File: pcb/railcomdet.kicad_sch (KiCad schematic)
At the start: 23 parts, among them J1 Screw_Terminal_01x04, J2 Screw_Terminal_01x02, J3 Screw_Terminal_01x08, U1 VO0631T, U15 VO0631T, U2 VO0631T

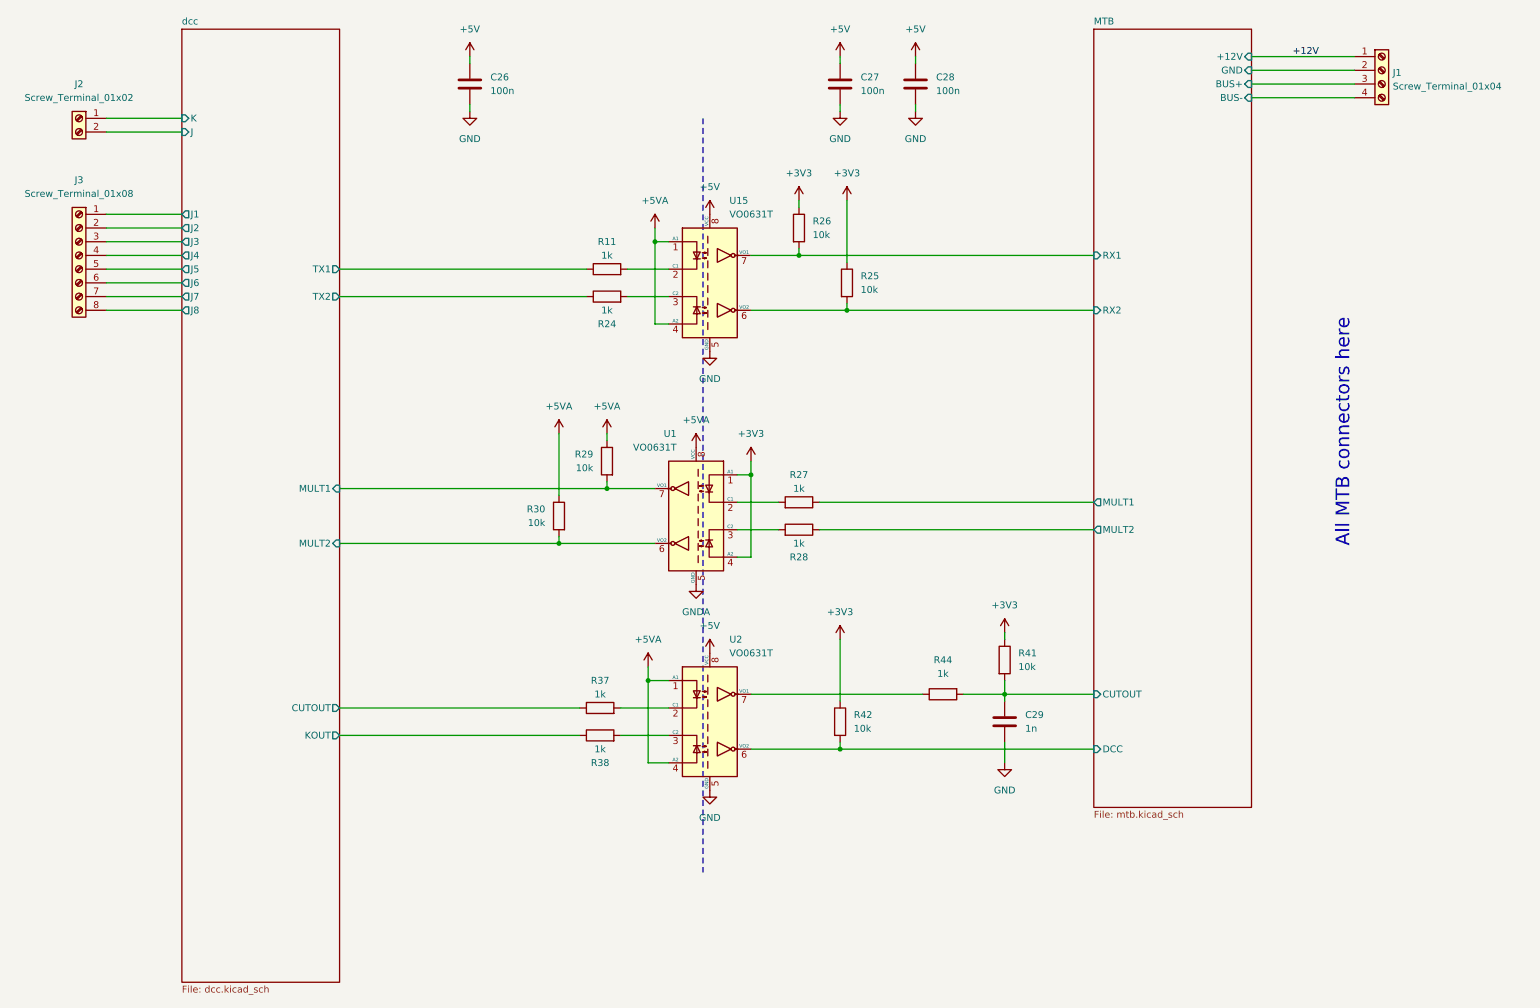
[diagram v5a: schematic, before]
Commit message: Added testpoints.
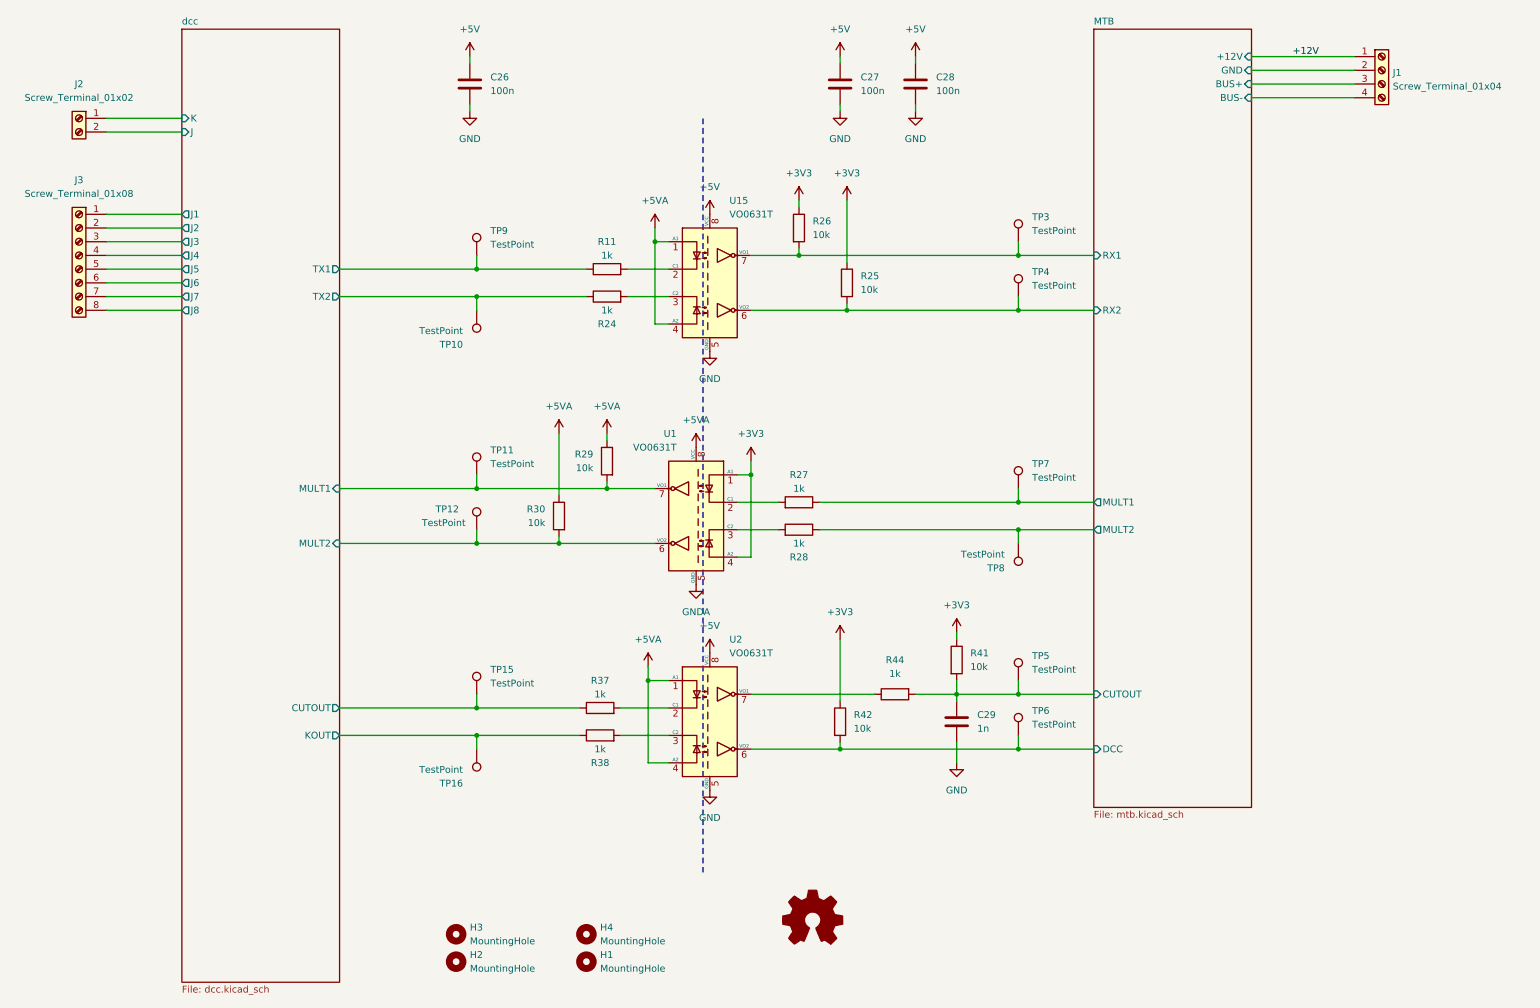
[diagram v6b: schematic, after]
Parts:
- added H1, H2, H3, H4: MountingHole, symbol Mechanical:MountingHole
- added TP10, TP11, TP12, TP15, TP16, TP3, TP4, TP5, TP6, TP7, TP8, TP9: TestPoint, symbol Connector:TestPoint
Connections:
- net MTB/CUTOUT: now also TP5.1
- net MTB/DCC: now also TP6.1
- net MTB/MULT1: now also TP7.1
- net MTB/MULT2: now also TP8.1
- net MTB/RX1: now also TP3.1
- net MTB/RX2: now also TP4.1
- net dcc/CUTOUT: now also TP15.1
- net dcc/KOUT: now also TP16.1
- net dcc/MULT1: now also TP11.1
- net dcc/MULT2: now also TP12.1
- net dcc/TX1: now also TP9.1
- net dcc/TX2: now also TP10.1
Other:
- note removed: "All MTB connectors here"
- moved on the sheet: C29, R41, R44

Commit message: Make ERC PASS.
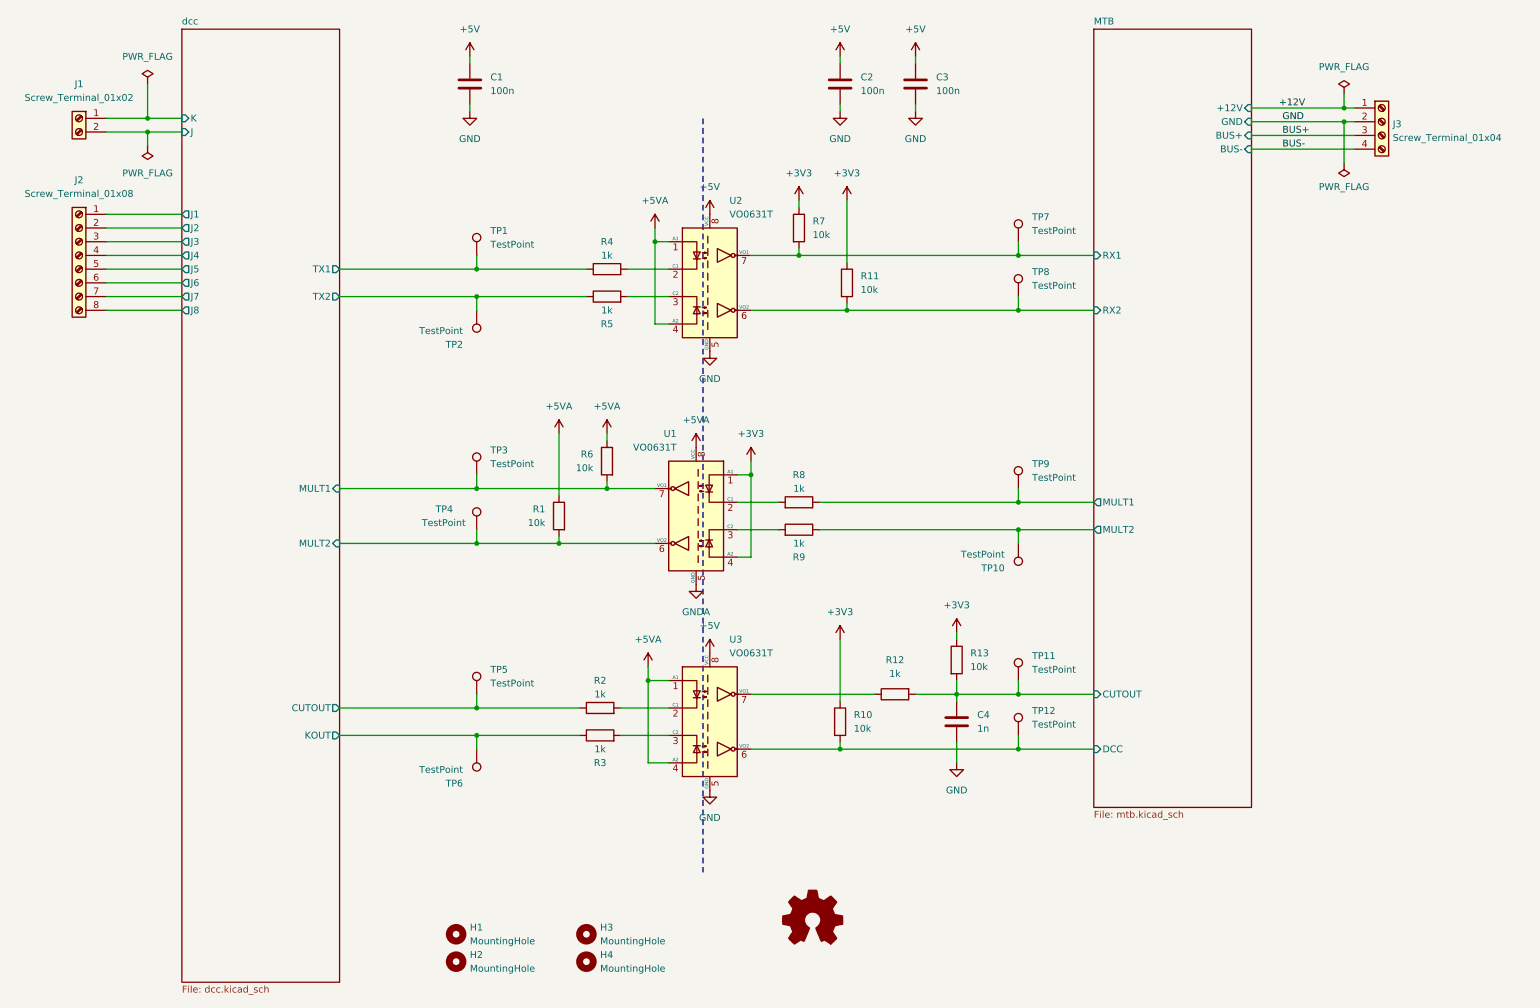
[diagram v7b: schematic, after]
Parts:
- renumbered C26 to C1, C27 to C2, C28 to C3, C29 to C4, H3 to H1, H4 to H3, H1 to H4, J2 to J1, J3 to J2, J1 to J3, R30 to R1, R42 to R10, R25 to R11, R44 to R12, R41 to R13, R37 to R2, R38 to R3, R11 to R4, R24 to R5, R29 to R6, R26 to R7, R27 to R8, R28 to R9, TP9 to TP1, TP8 to TP10, TP5 to TP11, TP6 to TP12, TP10 to TP2, TP11 to TP3, TP12 to TP4, TP15 to TP5, TP16 to TP6, TP3 to TP7, TP4 to TP8, TP7 to TP9, U15 to U2, U2 to U3
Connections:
- net MTB/GND is gone; now on net GND: J3.2 (Pin_2)
- net MTB/BUS+ renamed BUS+
- net MTB/BUS- renamed BUS-
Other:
- moved on the sheet: J3

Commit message: Added some footprints.
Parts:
- removed J2: Screw_Terminal_01x08, symbol Connector:Screw_Terminal_01x08
- removed J3: Screw_Terminal_01x04, symbol Connector:Screw_Terminal_01x04
- added J10, J2, J3, J7, J8, J9: MVE252-5-V, TerminalBlock:TerminalBlock_Altech_AK300-2_P5.00mm, symbol Connector:Screw_Terminal_01x02
- C1, C2, C3, C4: footprint (none) -> Capacitor_SMD:C_0805_2012Metric
- J1: value Screw_Terminal_01x02 -> MVE252-5-V; footprint (none) -> TerminalBlock:TerminalBlock_Altech_AK300-2_P5.00mm
- R1, R10, R11, R12, R13, R2, R3, R4, R5, R6, R7, R8, R9: footprint (none) -> Resistor_SMD:R_0805_2012Metric
- TP1, TP10, TP11, TP12, TP2, TP3, TP4, TP5, TP6, TP7, TP8, TP9: value TestPoint -> PAD; footprint (none) -> TestPoint:TestPoint_Pad_D2.0mm
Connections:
- net +12V: now also J3.1 (Pin_1)
- net BUS+: now also J10.1 (Pin_1)
- net BUS-: now also J10.2 (Pin_2)
- net GND: now also J3.2 (Pin_2)
- net dcc/J1: now also J2.1 (Pin_1)
- net dcc/J2: now also J2.2 (Pin_2)
- net dcc/J3: now also J7.1 (Pin_1)
- net dcc/J4: now also J7.2 (Pin_2)
- net dcc/J5: now also J8.1 (Pin_1)
- net dcc/J6: now also J8.2 (Pin_2)
- net dcc/J7: now also J9.1 (Pin_1)
- net dcc/J8: now also J9.2 (Pin_2)
